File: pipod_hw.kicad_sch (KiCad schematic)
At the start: 5 parts, among them J1 SFV8R-2STE1HLF, J2 SFV14R-2STE1HLF, J7 USB_C_Receptacle_USB2.0

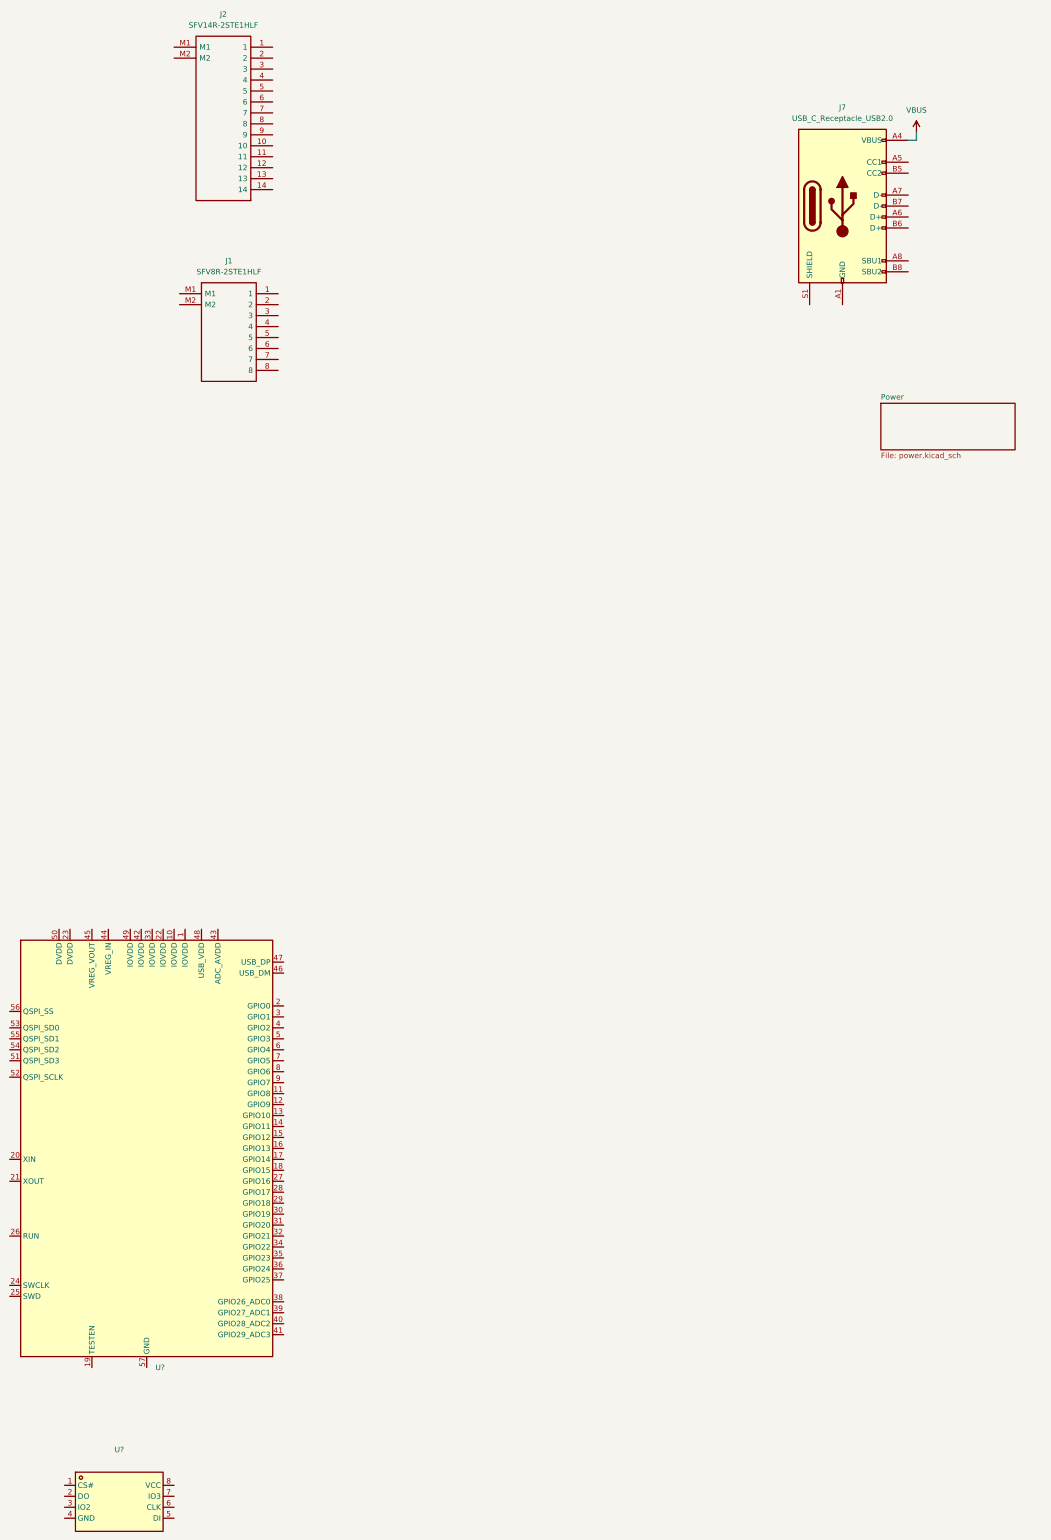
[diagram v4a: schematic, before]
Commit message: schem: digital design first pass
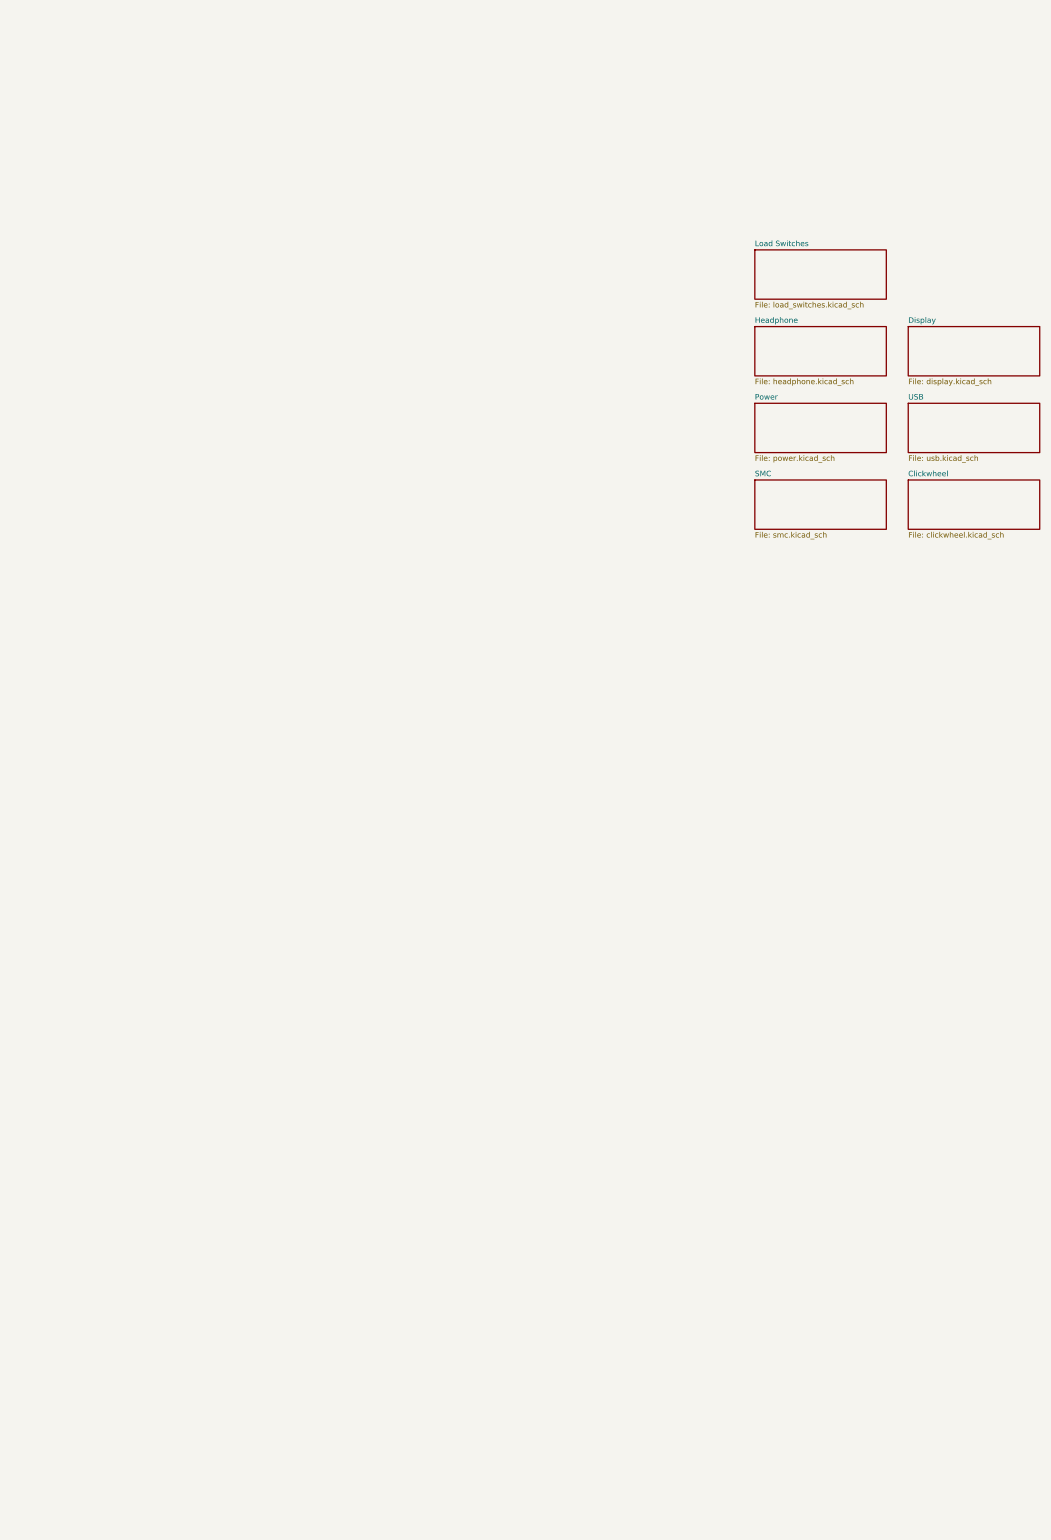
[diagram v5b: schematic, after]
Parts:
- removed J1: SFV8R-2STE1HLF, Gigahawk:SFV8R2STE1HLF, symbol gigahawk:SFV8R-2STE1HLF
- removed J2: SFV14R-2STE1HLF, Gigahawk:SFV14R2STE1HLF, symbol gigahawk:SFV14R-2STE1HLF
- removed J7: USB_C_Receptacle_USB2.0, Gigahawk:USB_C_Receptacle_GCT_USB4085, symbol Connector:USB_C_Receptacle_USB2.0
- removed U?: (no value), symbol lcsc:W25Q128JVSIQTR
- removed U?: (no value), symbol lcsc:RP2040
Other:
- added sheet Clickwheel (clickwheel.kicad_sch)
- added sheet Display (display.kicad_sch)
- added sheet Headphone (headphone.kicad_sch)
- added sheet Load Switches (load_switches.kicad_sch)
- added sheet SMC (smc.kicad_sch)
- added sheet USB (usb.kicad_sch)

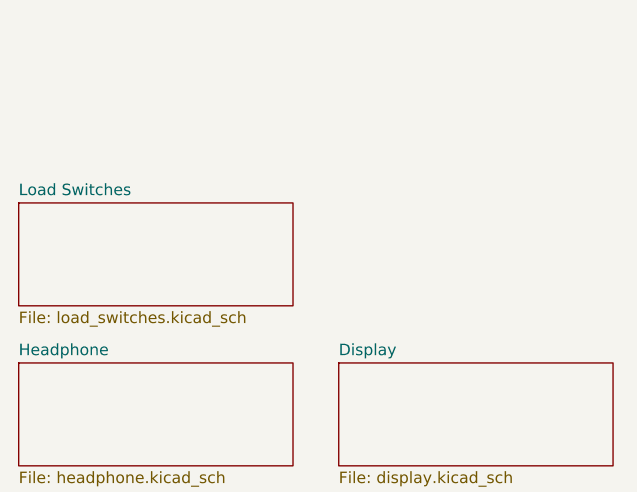
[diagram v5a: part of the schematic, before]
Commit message: schem: first pass done, ERC passing
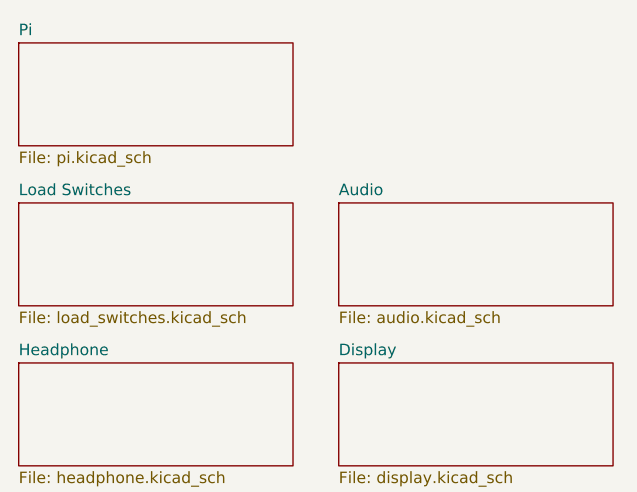
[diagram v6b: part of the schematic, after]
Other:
- added sheet Audio (audio.kicad_sch)
- added sheet Pi (pi.kicad_sch)
